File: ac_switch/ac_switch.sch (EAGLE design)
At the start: 21 parts, among them IC1 TINY85, T1 BC337, X2 SSW-102-02-S-S-RA

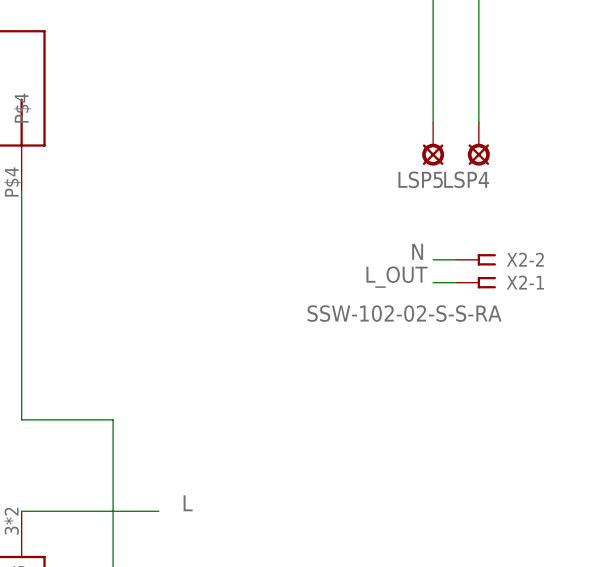
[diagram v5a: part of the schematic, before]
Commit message: Jetzt auch mit den richtigen Anschlussklemmen
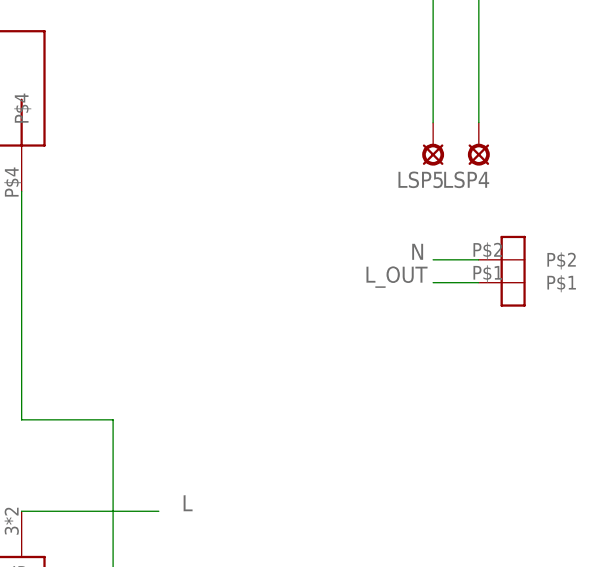
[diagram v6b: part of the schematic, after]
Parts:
- removed X2: SSW-102-02-S-S-RA, con-samtec:SSW-102-02-S-S-RA
- added U$6: WAGO_734_262, n39:WAGO_734_262
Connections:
- net L_OUT: now also U$6.P$1; no longer X2-1.1
- net N: now also U$6.P$2; no longer X2-2.1
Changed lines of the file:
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@@
 <grid distance="0.1" unitdist="inch" unit="inch" style="lines" multiple="1" display="no" altdistance="0.01" altunitdist="inch" altunit="inch"/>
 <layers>
-<layer number="1" name="Top" color="4" fill="1" visible="yes" active="no"/>
-<layer number="16" name="Bottom" color="1" fill="1" visible="yes" active="no"/>
-<layer number="17" name="Pads" color="2" fill="1" visible="yes" active="no"/>
-<layer number="18" name="Vias" color="2" fill="1" visible="yes" active="no"/>
-<layer number="19" name="Unrouted" color="6" fill="1" visible="yes" active="no"/>
-<layer number="20" name="Dimension" color="15" fill="1" visible="yes" active="no"/>
-<layer number="21" name="tPlace" color="7" fill="1" visible="yes" active="no"/>
-<layer number="22" name="bPlace" color="7" fill="1" visible="yes" active="no"/>
-<layer number="23" name="tOrigins" color="15" fill="1" visible="yes" active="no"/>
-<layer number="24" name="bOrigins" color="15" fill="1" visible="yes" active="no"/>
-<layer number="25" name="tNames" color="7" fill="1" visible="yes" active="no"/>
-<layer number="26" name="bNames" color="7" fill="1" visible="yes" active="no"/>
-<layer number="27" name="tValues" color="7" fill="1" visible="yes" active="no"/>
-<layer number="28" name="bValues" color="7" fill="1" visible="yes" active="no"/>
+<layer number="1" name="Top" color="4" fill="1" visible="no" active="no"/>
+<layer number="16" name="Bottom" color="1" fill="1" visible="no" active="no"/>
+<layer number="17" name="Pads" color="2" fill="1" visible="no" active="no"/>
+<layer number="18" name="Vias" color="2" fill="1" visible="no" active="no"/>
+<layer number="19" name="Unrouted" color="6" fill="1" visible="no" active="no"/>
+<layer number="20" name="Dimension" color="15" fill="1" visible="no" active="no"/>
+<layer number="21" name="tPlace" color="7" fill="1" visible="no" active="no"/>
+<layer number="22" name="bPlace" color="7" fill="1" visible="no" active="no"/>
+<layer number="23" name="tOrigins" color="15" fill="1" visible="no" active="no"/>
+<layer number="24" name="bOrigins" color="15" fill="1" visible="no" active="no"/>
+<layer number="25" name="tNames" color="7" fill="1" visible="no" active="no"/>
+<layer number="26" name="bNames" color="7" fill="1" visible="no" active="no"/>
+<layer number="27" name="tValues" color="7" fill="1" visible="no" active="no"/>
+<layer number="28" name="bValues" color="7" fill="1" visible="no" active="no"/>
 <layer number="29" name="tStop" color="7" fill="3" visible="no" active="no"/>
 <layer number="30" name="bStop" color="7" fill="6" visible="no" active="no"/>
@@
 <layer number="35" name="tGlue" color="7" fill="4" visible="no" active="no"/>
 <layer number="36" name="bGlue" color="7" fill="5" visible="no" active="no"/>
-<layer number="37" name="tTest" color="7" fill="1" visible="yes" active="no"/>
-<layer number="38" name="bTest" color="7" fill="1" visible="yes" active="no"/>
+<layer number="37" name="tTest" color="7" fill="1" visible="no" active="no"/>
+<layer number="38" name="bTest" color="7" fill="1" visible="no" active="no"/>
 <layer number="39" name="tKeepout" color="4" fill="11" visible="no" active="no"/>
 <layer number="40" name="bKeepout" color="1" fill="11" visible="no" active="no"/>
@@
 <layer number="44" name="Drills" color="7" fill="1" visible="no" active="no"/>
 <layer number="45" name="Holes" color="7" fill="1" visible="no" active="no"/>
-<layer number="46" name="Milling" color="3" fill="1" visible="yes" active="no"/>
-<layer number="47" name="Measures" color="7" fill="1" visible="yes" active="no"/>
-<layer number="48" name="Document" color="7" fill="1" visible="yes" active="no"/>
-<layer number="49" name="Reference" color="7" fill="1" visible="yes" active="no"/>
-<layer number="51" name="tDocu" color="7" fill="1" visible="yes" active="no"/>
-<layer number="52" name="bDocu" color="7" fill="1" visible="yes" active="no"/>
+<layer number="46" name="Milling" color="3" fill="1" visible="no" active="no"/>
+<layer number="47" name="Measures" color="7" fill="1" visible="no" active="no"/>
+<layer number="48" name="Document" color="7" fill="1" visible="no" active="no"/>
+<layer number="49" name="Reference" color="7" fill="1" visible="no" active="no"/>
+<layer number="51" name="tDocu" color="7" fill="1" visible="no" active="no"/>
+<layer number="52" name="bDocu" color="7" fill="1" visible="no" active="no"/>
 <layer number="91" name="Nets" color="2" fill="1" visible="yes" active="yes"/>
 <layer number="92" name="Busses" color="1" fill="1" visible="yes" active="yes"/>
@@
 <part name="C4" library="resistor" deviceset="CPOL-EU" device="E3.5-8" value="68µ"/>
 <part name="U$5" library="n39" deviceset="I3C_PORT" device=""/>
-<part name="X2" library="con-samtec" deviceset="SSW-102-02-S-S" device="-RA"/>
 <part name="R3" library="resistor" deviceset="R-EU_" device="0204/7" value="1,5K"/>
+<part name="U$6" library="n39" deviceset="WAGO_734_262" device=""/>
 </parts>
 <sheets>
@@
 <instance part="C4" gate="G$1" x="-12.7" y="76.2"/>
 <instance part="U$5" gate="G$1" x="-60.96" y="-17.78"/>
-<instance part="X2" gate="-1" x="129.54" y="20.32" rot="R180"/>
-<instance part="X2" gate="-2" x="129.54" y="22.86" rot="R180"/>
 <instance part="R3" gate="G$1" x="35.56" y="17.78" rot="R180"/>
+<instance part="U$6" gate="G$1" x="132.08" y="22.86" rot="R90"/>
 </instances>
 <busses>
@@
 </segment>
 <segment>
-<pinref part="X2" gate="-2" pin="1"/>
-<wire x1="127" y1="22.86" x2="124.46" y2="22.86" width="0.1524" layer="91"/>
 <label x="121.92" y="22.86" size="1.778" layer="95"/>
+<pinref part="U$6" gate="G$1" pin="P$2"/>
+<wire x1="124.46" y1="22.86" x2="129.54" y2="22.86" width="0.1524" layer="91"/>
 </segment>
 </net>
@@
 </segment>
 <segment>
-<pinref part="X2" gate="-1" pin="1"/>
-<wire x1="127" y1="20.32" x2="124.46" y2="20.32" width="0.1524" layer="91"/>
 <label x="116.84" y="20.32" size="1.778" layer="95"/>
-</segment>
-</net>
+<pinref part="U$6" gate="G$1" pin="P$1"/>
+<wire x1="124.46" y1="20.32" x2="129.54" y2="20.32" width="0.1524" layer="91"/>
+</segment>
+</net>

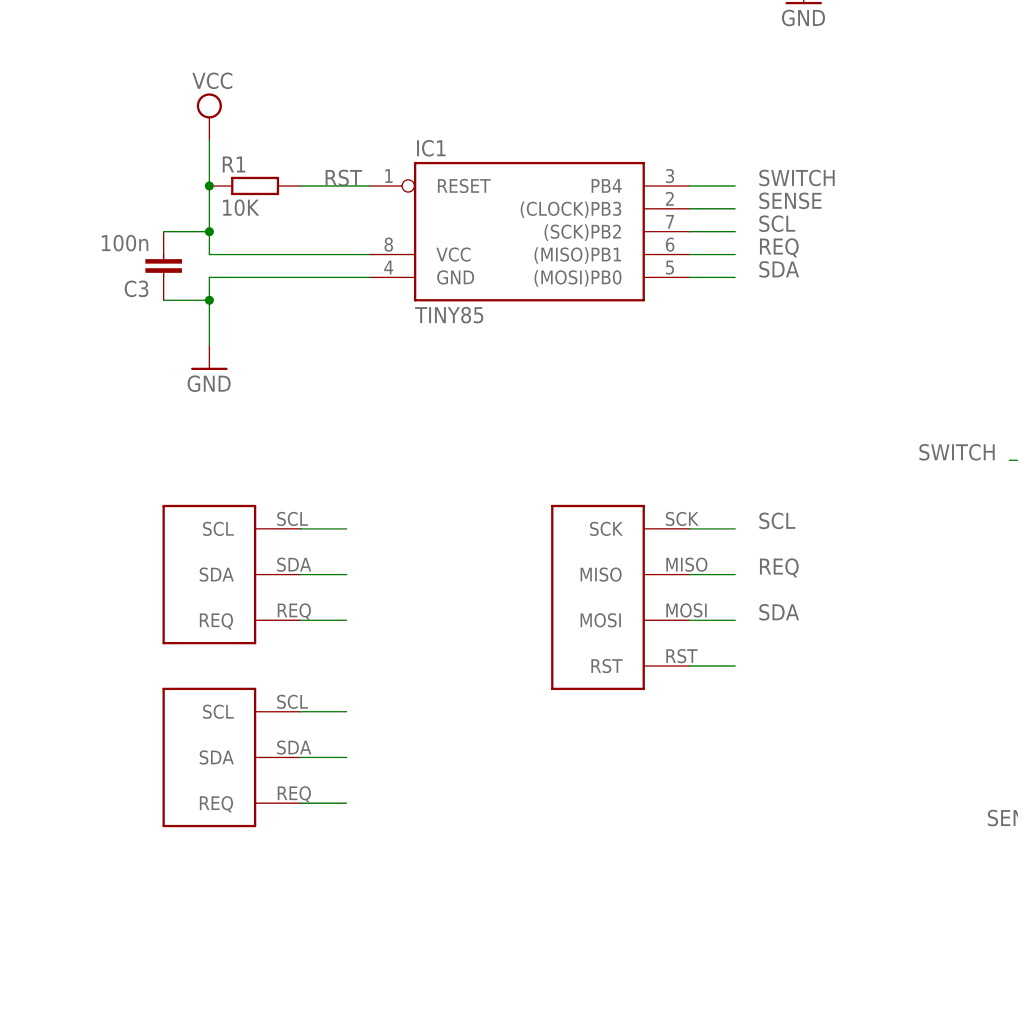
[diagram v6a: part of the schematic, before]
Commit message: Platinenlayout angepasst, sodass es zum Power-Board passt
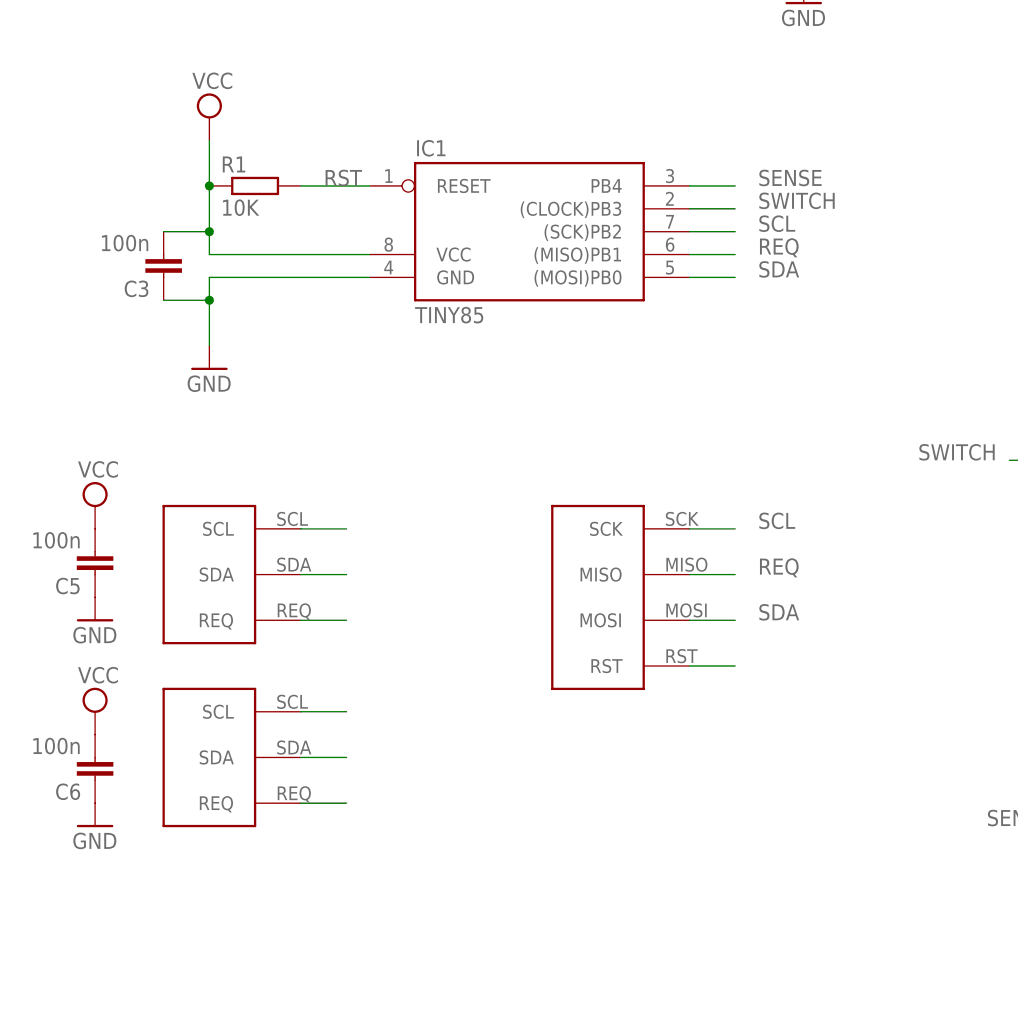
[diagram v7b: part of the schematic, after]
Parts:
- added C5, C6: 100n, resistor:C-EU025-024X044
- LED1: device led:LED5MM -> led:LED3MM
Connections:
- net GND: now also C5.1, C6.1
- net SENSE: now also IC1.PB4; no longer IC1.(CLOCK)PB3
- net SWITCH: now also IC1.(CLOCK)PB3; no longer IC1.PB4
- net VCC: now also C5.2, C6.2
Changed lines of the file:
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@@
 <part name="C3" library="resistor" deviceset="C-EU" device="025-024X044" value="100n"/>
 <part name="R1" library="resistor" deviceset="R-EU_" device="0207/10" value="10K"/>
-<part name="LED1" library="led" deviceset="LED" device="5MM"/>
+<part name="LED1" library="led" deviceset="LED" device="3MM"/>
 <part name="R2" library="resistor" deviceset="R-EU_" device="0204/7" value="220R"/>
 <part name="U$3" library="n39" deviceset="I3C_PORT" device=""/>
@@
 <part name="R3" library="resistor" deviceset="R-EU_" device="0204/7" value="1,5K"/>
 <part name="U$6" library="n39" deviceset="WAGO_734_262" device=""/>
+<part name="C5" library="resistor" deviceset="C-EU" device="025-024X044" value="100n"/>
+<part name="C6" library="resistor" deviceset="C-EU" device="025-024X044" value="100n"/>
+<part name="GND5" library="supply1" deviceset="GND" device=""/>
+<part name="SUPPLY5" library="supply2" deviceset="VCC" device=""/>
+<part name="SUPPLY6" library="supply2" deviceset="VCC" device=""/>
+<part name="GND6" library="supply1" deviceset="GND" device=""/>
 </parts>
 <sheets>
@@
 <instance part="R3" gate="G$1" x="35.56" y="17.78" rot="R180"/>
 <instance part="U$6" gate="G$1" x="132.08" y="22.86" rot="R90"/>
+<instance part="C5" gate="G$1" x="-73.66" y="5.08" rot="R180"/>
+<instance part="C6" gate="G$1" x="-73.66" y="-17.78" rot="R180"/>
+<instance part="GND5" gate="1" x="-73.66" y="0"/>
+<instance part="SUPPLY5" gate="G$1" x="-73.66" y="12.7"/>
+<instance part="SUPPLY6" gate="G$1" x="-73.66" y="-10.16"/>
+<instance part="GND6" gate="1" x="-73.66" y="-22.86"/>
 </instances>
 <busses>
@@
 <wire x1="45.72" y1="58.42" x2="45.72" y2="45.72" width="0.1524" layer="91"/>
 </segment>
+<segment>
+<pinref part="C5" gate="G$1" pin="2"/>
+<pinref part="SUPPLY5" gate="G$1" pin="VCC"/>
+</segment>
+<segment>
+<pinref part="C6" gate="G$1" pin="2"/>
+<pinref part="SUPPLY6" gate="G$1" pin="VCC"/>
+</segment>
 </net>
 <net name="GND" class="0">
@@
 <wire x1="53.34" y1="7.62" x2="53.34" y2="12.7" width="0.1524" layer="91"/>
 </segment>
+<segment>
+<pinref part="C5" gate="G$1" pin="1"/>
+<pinref part="GND5" gate="1" pin="GND"/>
+</segment>
+<segment>
+<pinref part="GND6" gate="1" pin="GND"/>
+<pinref part="C6" gate="G$1" pin="1"/>
+</segment>
 </net>
 <net name="N$2" class="0">
@@
 <net name="SWITCH" class="0">
 <segment>
+<pinref part="R3" gate="G$1" pin="2"/>
+<wire x1="30.48" y1="17.78" x2="27.94" y2="17.78" width="0.1524" layer="91"/>
+<label x="17.78" y="17.78" size="1.778" layer="95"/>
+</segment>
+<segment>
+<pinref part="IC1" gate="G$1" pin="(CLOCK)PB3"/>
+<wire x1="-7.62" y1="45.72" x2="-2.54" y2="45.72" width="0.1524" layer="91"/>
+<label x="0" y="45.72" size="1.778" layer="95"/>
+</segment>
+</net>
+<net name="SENSE" class="0">
+<segment>
+<pinref part="U$2" gate="ACS714" pin="VOUT"/>
+<wire x1="63.5" y1="-22.86" x2="35.56" y2="-22.86" width="0.1524" layer="91"/>
+<label x="25.4" y="-22.86" size="1.778" layer="95"/>
+</segment>
+<segment>
 <pinref part="IC1" gate="G$1" pin="PB4"/>
 <wire x1="-7.62" y1="48.26" x2="-2.54" y2="48.26" width="0.1524" layer="91"/>
 <label x="0" y="48.26" size="1.778" layer="95"/>
 </segment>
-<segment>
-<pinref part="R3" gate="G$1" pin="2"/>
-<wire x1="30.48" y1="17.78" x2="27.94" y2="17.78" width="0.1524" layer="91"/>
-<label x="17.78" y="17.78" size="1.778" layer="95"/>
-</segment>
-</net>
-<net name="SENSE" class="0">
-<segment>
-<pinref part="U$2" gate="ACS714" pin="VOUT"/>
-<wire x1="63.5" y1="-22.86" x2="35.56" y2="-22.86" width="0.1524" layer="91"/>
-<label x="25.4" y="-22.86" size="1.778" layer="95"/>
-</segment>
-<segment>
-<pinref part="IC1" gate="G$1" pin="(CLOCK)PB3"/>
-<wire x1="-7.62" y1="45.72" x2="-2.54" y2="45.72" width="0.1524" layer="91"/>
-<label x="0" y="45.72" size="1.778" layer="95"/>
-</segment>
-</net>
+</net>
